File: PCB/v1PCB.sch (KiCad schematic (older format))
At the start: 223 parts, among them SW1 SW_PUSH, SW2 SW_PUSH, U1 STM32F072CBUx, U2 MCP1700-3302E_SOT23

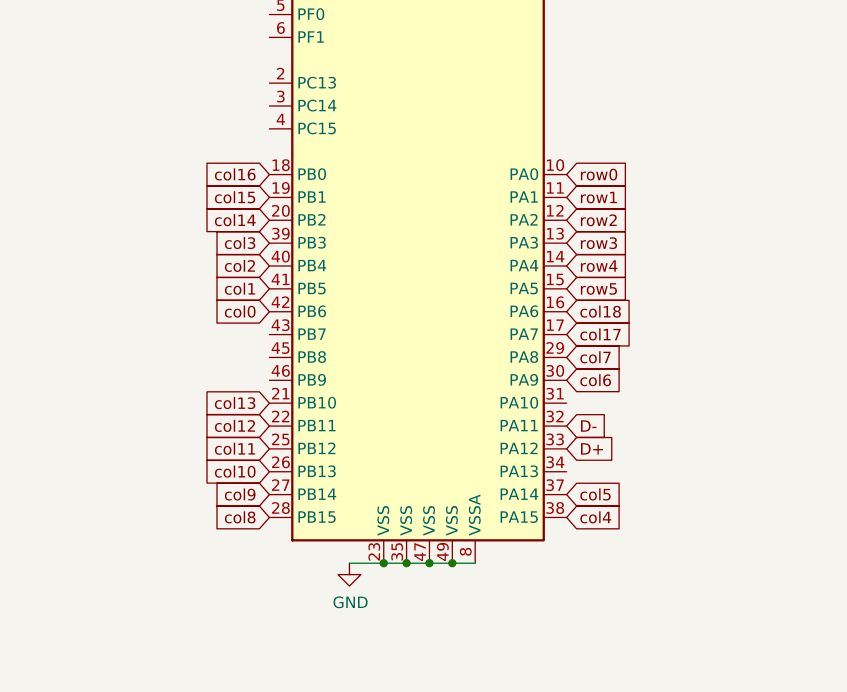
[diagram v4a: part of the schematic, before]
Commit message: Redo all traces because MCU got moved to bottom. Continue refining CAD model.
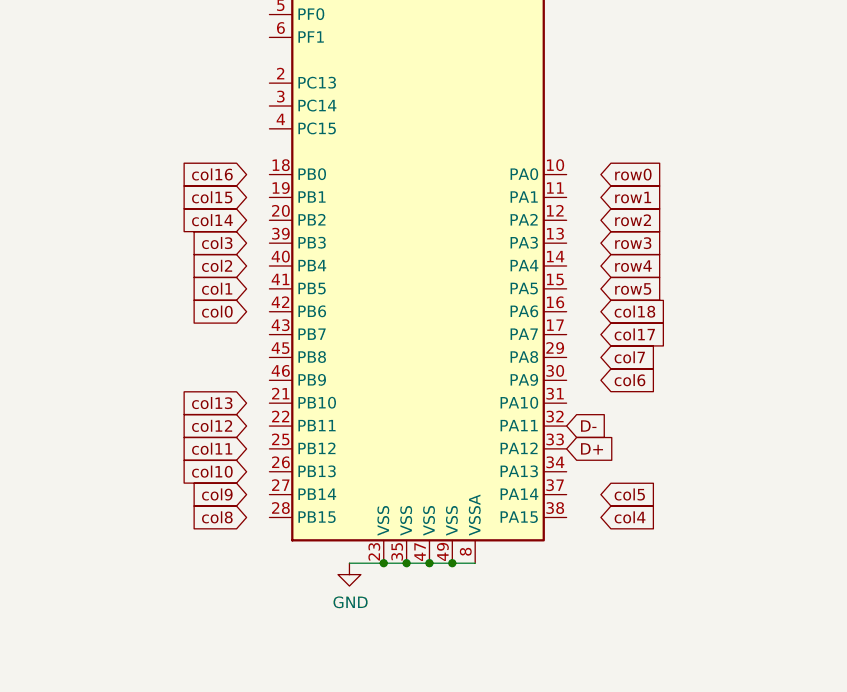
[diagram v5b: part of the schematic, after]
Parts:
- K_32, K_54, K_87: footprint MX_Only:MXOnly-1U-NoLED -> MX_Only:MXOnly-2U-NoLED
- K_67, K_71, K_91: footprint MX_Only:MXOnly-1U-NoLED -> MX_Only:MXOnly-2.25U-NoLED
- K_82: footprint MX_Only:MXOnly-1U-NoLED -> MX_Only:MXOnly-1.75U-NoLED
- K_93: footprint MX_Only:MXOnly-1U-NoLED -> MX_Only:MXOnly-3U-NoLED
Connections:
- net col0: no longer U1.42 (PB6)
- net col1: no longer U1.41 (PB5)
- net col10: no longer U1.26 (PB13)
- net col11: no longer U1.25 (PB12)
- net col12: no longer U1.22 (PB11)
- net col13: no longer U1.21 (PB10)
- net col14: no longer U1.20 (PB2)
- net col15: no longer U1.19 (PB1)
- net col16: no longer U1.18 (PB0)
- net col17: no longer U1.17 (PA7)
- net col18: no longer U1.16 (PA6)
- net col2: no longer U1.40 (PB4)
- net col3: no longer U1.39 (PB3)
- net col4: no longer U1.38 (PA15)
- net col5: no longer U1.37 (PA14)
- net col6: no longer U1.30 (PA9)
- net col7: no longer U1.29 (PA8)
- net col8: no longer U1.28 (PB15)
- net col9: no longer U1.27 (PB14)
- net row0: no longer U1.10 (PA0)
- net row1: no longer U1.11 (PA1)
- net row2: no longer U1.12 (PA2)
- net row3: no longer U1.13 (PA3)
- net row4: no longer U1.14 (PA4)
- net row5: no longer U1.15 (PA5)
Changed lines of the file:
@@
 F 0 "K_32" H 16450 7033 60  0000 C CNN
 F 1 "KEYSW" H 16450 6700 60  0001 C CNN
-F 2 "MX_Only:MXOnly-1U-NoLED" H 16450 6800 60  0001 C CNN
+F 2 "MX_Only:MXOnly-2U-NoLED" H 16450 6800 60  0001 C CNN
 F 3 "" H 16450 6800 60  0000 C CNN
 	1    16450 6800
@@
 F 0 "K_67" H 15450 9033 60  0000 C CNN
 F 1 "KEYSW" H 15450 8700 60  0001 C CNN
-F 2 "MX_Only:MXOnly-1U-NoLED" H 15450 8800 60  0001 C CNN
+F 2 "MX_Only:MXOnly-2.25U-NoLED" H 15450 8800 60  0001 C CNN
 F 3 "" H 15450 8800 60  0000 C CNN
 	1    15450 8800
@@
 F 0 "K_54" H 20450 9033 60  0000 C CNN
 F 1 "KEYSW" H 20450 8700 60  0001 C CNN
-F 2 "MX_Only:MXOnly-1U-NoLED" H 20450 8800 60  0001 C CNN
+F 2 "MX_Only:MXOnly-2U-NoLED" H 20450 8800 60  0001 C CNN
 F 3 "" H 20450 8800 60  0000 C CNN
 	1    20450 8800
@@
 F 0 "K_82" H 15450 10033 60  0000 C CNN
 F 1 "KEYSW" H 15450 9700 60  0001 C CNN
-F 2 "MX_Only:MXOnly-1U-NoLED" H 15450 9800 60  0001 C CNN
+F 2 "MX_Only:MXOnly-1.75U-NoLED" H 15450 9800 60  0001 C CNN
 F 3 "" H 15450 9800 60  0000 C CNN
 	1    15450 9800
@@
 F 0 "K_91" H 6450 11033 60  0000 C CNN
 F 1 "KEYSW" H 6450 10700 60  0001 C CNN
-F 2 "MX_Only:MXOnly-1U-NoLED" H 6450 10800 60  0001 C CNN
+F 2 "MX_Only:MXOnly-2.25U-NoLED" H 6450 10800 60  0001 C CNN
 F 3 "" H 6450 10800 60  0000 C CNN
 	1    6450 10800
@@
 F 0 "K_93" H 10450 11033 60  0000 C CNN
 F 1 "KEYSW" H 10450 10700 60  0001 C CNN
-F 2 "MX_Only:MXOnly-1U-NoLED" H 10450 10800 60  0001 C CNN
+F 2 "MX_Only:MXOnly-3U-NoLED" H 10450 10800 60  0001 C CNN
 F 3 "" H 10450 10800 60  0000 C CNN
 	1    10450 10800
@@
 F 0 "K_87" H 20450 11033 60  0000 C CNN
 F 1 "KEYSW" H 20450 10700 60  0001 C CNN
-F 2 "MX_Only:MXOnly-1U-NoLED" H 20450 10800 60  0001 C CNN
+F 2 "MX_Only:MXOnly-2U-NoLED" H 20450 10800 60  0001 C CNN
 F 3 "" H 20450 10800 60  0000 C CNN
 	1    20450 10800
@@
 	1    0    0    -1
 $EndComp
-Text GLabel 10500 2700 0    50   Input ~ 0
+Text GLabel 10400 2700 0    50   Input ~ 0
 col3
-Text GLabel 11800 3900 2    50   Input ~ 0
+Text GLabel 11950 3900 2    50   Input ~ 0
 col4
-Text GLabel 11800 3800 2    50   Input ~ 0
+Text GLabel 11950 3800 2    50   Input ~ 0
 col5
-Text GLabel 11800 3300 2    50   Input ~ 0
+Text GLabel 11950 3300 2    50   Input ~ 0
 col6
-Text GLabel 11800 3200 2    50   Input ~ 0
+Text GLabel 11950 3200 2    50   Input ~ 0
 col7
-Text GLabel 10500 3400 0    50   Input ~ 0
+Text GLabel 10400 3400 0    50   Input ~ 0
 col13
-Text GLabel 10500 2600 0    50   Input ~ 0
+Text GLabel 10400 2600 0    50   Input ~ 0
 col14
-Text GLabel 10500 2500 0    50   Input ~ 0
+Text GLabel 10400 2500 0    50   Input ~ 0
 col15
-Text GLabel 10500 2800 0    50   Input ~ 0
+Text GLabel 10400 2800 0    50   Input ~ 0
 col2
 Connection ~ 11100 1100
@@
 	1    0    0    -1
 $EndComp
-Text GLabel 10500 3000 0    50   Input ~ 0
+Text GLabel 10400 3000 0    50   Input ~ 0
 col0
-Text GLabel 10500 2900 0    50   Input ~ 0
+Text GLabel 10400 2900 0    50   Input ~ 0
 col1
-Text GLabel 11800 2900 2    50   Input ~ 0
+Text GLabel 11950 2900 2    50   Input ~ 0
 row5
 Connection ~ 5200 2000
@@
 F 0 "K_71" H 3450 10033 60  0000 C CNN
 F 1 "KEYSW" H 3450 9700 60  0001 C CNN
-F 2 "MX_Only:MXOnly-1U-NoLED" H 3450 9800 60  0001 C CNN
+F 2 "MX_Only:MXOnly-2.25U-NoLED" H 3450 9800 60  0001 C CNN
 F 3 "" H 3450 9800 60  0000 C CNN
 	1    3450 9800
@@
 	20050 9200 20400 9200
 Connection ~ 19400 8200
-Text GLabel 10500 3600 0    50   Input ~ 0
+Text GLabel 10400 3600 0    50   Input ~ 0
 col11
-Text GLabel 10500 3900 0    50   Input ~ 0
+Text GLabel 10400 3900 0    50   Input ~ 0
 col8
-Text GLabel 10500 3500 0    50   Input ~ 0
+Text GLabel 10400 3500 0    50   Input ~ 0
 col12
-Text GLabel 10500 3700 0    50   Input ~ 0
+Text GLabel 10400 3700 0    50   Input ~ 0
 col10
-Text GLabel 10500 3800 0    50   Input ~ 0
+Text GLabel 10400 3800 0    50   Input ~ 0
 col9
-Text GLabel 11800 2400 2    50   Input ~ 0
+Text GLabel 11950 2400 2    50   Input ~ 0
 row0
-Text GLabel 11800 2500 2    50   Input ~ 0
+Text GLabel 11950 2500 2    50   Input ~ 0
 row1
-Text GLabel 11800 2600 2    50   Input ~ 0
+Text GLabel 11950 2600 2    50   Input ~ 0
 row2
-Text GLabel 11800 2700 2    50   Input ~ 0
+Text GLabel 11950 2700 2    50   Input ~ 0
 row3
-Text GLabel 11800 2800 2    50   Input ~ 0
+Text GLabel 11950 2800 2    50   Input ~ 0
 row4
-Text GLabel 11800 3000 2    50   Input ~ 0
+Text GLabel 11950 3000 2    50   Input ~ 0
 col18
-Text GLabel 11800 3100 2    50   Input ~ 0
+Text GLabel 11950 3100 2    50   Input ~ 0
 col17
-Text GLabel 10500 2400 0    50   Input ~ 0
+Text GLabel 10400 2400 0    50   Input ~ 0
 col16
 Text GLabel 11800 3600 2    50   Input ~ 0

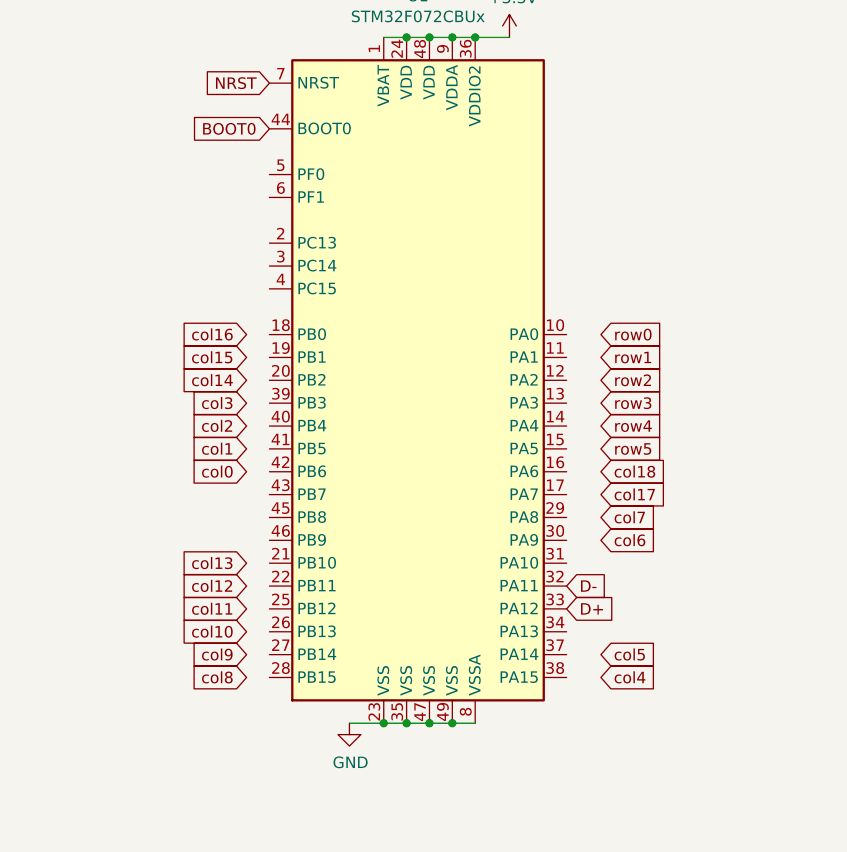
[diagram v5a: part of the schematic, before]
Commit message: Finished relocating MCU, prep for review. Need to adjust cutouts for case mounting.
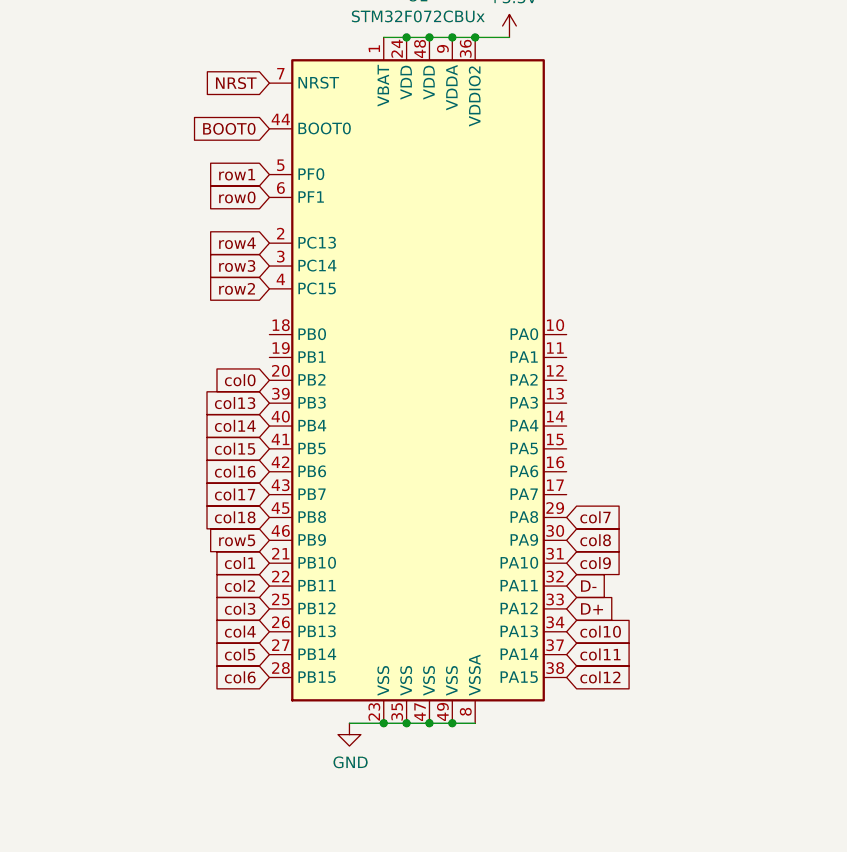
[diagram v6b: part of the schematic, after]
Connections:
- net col0: now also U1.20 (PB2)
- net col1: now also U1.21 (PB10)
- net col10: now also U1.34 (PA13)
- net col11: now also U1.37 (PA14)
- net col12: now also U1.38 (PA15)
- net col13: now also U1.39 (PB3)
- net col14: now also U1.40 (PB4)
- net col15: now also U1.41 (PB5)
- net col16: now also U1.42 (PB6)
- net col17: now also U1.43 (PB7)
- net col18: now also U1.45 (PB8)
- net col2: now also U1.22 (PB11)
- net col3: now also U1.25 (PB12)
- net col4: now also U1.26 (PB13)
- net col5: now also U1.27 (PB14)
- net col6: now also U1.28 (PB15)
- net col7: now also U1.29 (PA8)
- net col8: now also U1.30 (PA9)
- net col9: now also U1.31 (PA10)
- net row0: now also U1.6 (PF1)
- net row1: now also U1.5 (PF0)
- net row2: now also U1.4 (PC15)
- net row3: now also U1.3 (PC14)
- net row4: now also U1.2 (PC13)
- net row5: now also U1.46 (PB9)
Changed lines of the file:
@@
 	1    0    0    -1
 $EndComp
-Text GLabel 10400 2700 0    50   Input ~ 0
+Text GLabel 10500 3600 0    50   Input ~ 0
 col3
-Text GLabel 11950 3900 2    50   Input ~ 0
+Text GLabel 10500 3700 0    50   Input ~ 0
 col4
-Text GLabel 11950 3800 2    50   Input ~ 0
+Text GLabel 10500 3800 0    50   Input ~ 0
 col5
-Text GLabel 11950 3300 2    50   Input ~ 0
+Text GLabel 10500 3900 0    50   Input ~ 0
 col6
-Text GLabel 11950 3200 2    50   Input ~ 0
+Text GLabel 11800 3200 2    50   Input ~ 0
 col7
-Text GLabel 10400 3400 0    50   Input ~ 0
+Text GLabel 10500 2700 0    50   Input ~ 0
 col13
-Text GLabel 10400 2600 0    50   Input ~ 0
+Text GLabel 10500 2800 0    50   Input ~ 0
 col14
-Text GLabel 10400 2500 0    50   Input ~ 0
+Text GLabel 10500 2900 0    50   Input ~ 0
 col15
-Text GLabel 10400 2800 0    50   Input ~ 0
+Text GLabel 10500 3500 0    50   Input ~ 0
 col2
 Connection ~ 11100 1100
@@
 	1    0    0    -1
 $EndComp
-Text GLabel 10400 3000 0    50   Input ~ 0
+Text GLabel 10500 2600 0    50   Input ~ 0
 col0
-Text GLabel 10400 2900 0    50   Input ~ 0
+Text GLabel 10500 3400 0    50   Input ~ 0
 col1
-Text GLabel 11950 2900 2    50   Input ~ 0
+Text GLabel 10500 3300 0    50   Input ~ 0
 row5
 Connection ~ 5200 2000
@@
 	20050 9200 20400 9200
 Connection ~ 19400 8200
-Text GLabel 10400 3600 0    50   Input ~ 0
+Text GLabel 11800 3800 2    50   Input ~ 0
 col11
-Text GLabel 10400 3900 0    50   Input ~ 0
+Text GLabel 11800 3300 2    50   Input ~ 0
 col8
-Text GLabel 10400 3500 0    50   Input ~ 0
+Text GLabel 11800 3900 2    50   Input ~ 0
 col12
-Text GLabel 10400 3700 0    50   Input ~ 0
+Text GLabel 11800 3700 2    50   Input ~ 0
 col10
-Text GLabel 10400 3800 0    50   Input ~ 0
+Text GLabel 11800 3400 2    50   Input ~ 0
 col9
-Text GLabel 11950 2400 2    50   Input ~ 0
+Text GLabel 10500 1800 0    50   Input ~ 0
 row0
-Text GLabel 11950 2500 2    50   Input ~ 0
+Text GLabel 10500 1700 0    50   Input ~ 0
 row1
-Text GLabel 11950 2600 2    50   Input ~ 0
+Text GLabel 10500 2200 0    50   Input ~ 0
 row2
-Text GLabel 11950 2700 2    50   Input ~ 0
+Text GLabel 10500 2100 0    50   Input ~ 0
 row3
-Text GLabel 11950 2800 2    50   Input ~ 0
+Text GLabel 10500 2000 0    50   Input ~ 0
 row4
-Text GLabel 11950 3000 2    50   Input ~ 0
+Text GLabel 10500 3200 0    50   Input ~ 0
 col18
-Text GLabel 11950 3100 2    50   Input ~ 0
+Text GLabel 10500 3100 0    50   Input ~ 0
 col17
-Text GLabel 10400 2400 0    50   Input ~ 0
+Text GLabel 10500 3000 0    50   Input ~ 0
 col16
 Text GLabel 11800 3600 2    50   Input ~ 0
